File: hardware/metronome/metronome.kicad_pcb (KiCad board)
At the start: 2 copper layers, 59 x 34 mm, 57 parts, among them J1 USB_C_Receptacle_USB2.0, J2 Conn_01x03_Pin, J3 Conn_01x04_Pin, J4 AudioJack3_Ground, SW1 RotaryEncoder_Switch, SW2 SW_SPST, SW3 SW_SPST, SW4 SW_SPST, SW5 SW_SPST, U1 ATtiny412, U2 ME6209A40PG, U3 FM8002, Y1 10MHz

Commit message: Version 02
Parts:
- removed H1: MountingHole, MountingHole:MountingHole_2.2mm_M2
- added C13: 100uF, Capacitor_SMD:CP_Elec_6.3x5.4_Nichicon, F.Cu at (155.7, 67.0)
- added C14: 2.2uF, Capacitor_SMD:C_0805_2012Metric_Pad1.18x1.45mm_HandSolder, F.Cu at (136.7, 68.6)
- added C15: 0.1uF, Capacitor_SMD:C_0603_1608Metric_Pad1.08x0.95mm_HandSolder, F.Cu at (145.6, 61.7)
- added R30: 3k9, Resistor_SMD:R_0603_1608Metric_Pad0.98x0.95mm_HandSolder, F.Cu at (141.1, 63.5)
- added R31: 3k9, Resistor_SMD:R_0603_1608Metric_Pad0.98x0.95mm_HandSolder, F.Cu at (150.1, 70.6)
- added R32: 3k9, Resistor_SMD:R_0603_1608Metric_Pad0.98x0.95mm_HandSolder, F.Cu at (145.7, 70.6)
- C10: value 1.0uF -> 1uF
- C11: value 0.33uF -> 100uF; footprint Capacitor_SMD:C_0603_1608Metric_Pad1.08x0.95mm_HandSolder -> Capacitor_SMD:CP_Elec_6.3x5.4_Nichicon
- C12: value 1.0uF -> 2.2uF; footprint Capacitor_SMD:C_0603_1608Metric_Pad1.08x0.95mm_HandSolder -> Capacitor_SMD:C_0805_2012Metric_Pad1.18x1.45mm_HandSolder
- J2: value Conn_01x03_Pin -> Conn_01x04_Pin; footprint Connector_PinHeader_2.54mm:PinHeader_1x03_P2.54mm_Vertical -> ELonginus:1x4_2.54mm_pin_staggered
- J4: footprint ELonginus:Jack_3.5mm_PJ320E_Horizontal -> ELonginus:6.35mm headphone jack PJ-611A
- R26: value 10k -> 100k
- R27: value 20k -> 100k
- R28: value 20k -> 3k9
- SW2, SW3: footprint Button_Switch_THT:SW_PUSH_6mm_H4.3mm -> ELonginus:SW_PUSH_6mm
- SW4, SW5: footprint Button_Switch_THT:SW_PUSH-12mm -> ELonginus:SW_PUSH_12mm
- U3: value FM8002 -> LM4808; footprint Package_SO:SOP-8-1EP_4.57x4.57mm_P1.27mm_EP4.57x4.45mm_ThermalVias -> Package_SO:SOIC-8_3.9x4.9mm_P1.27mm
- moved C11 30.4 mm to (163.1, 67.0), turned to 90 degrees
- moved R21 19.1 mm to (150.0, 85.1), turned to 0 degrees
- moved C5 17.6 mm to (145.9, 85.1), turned to 180 degrees
- moved C12 15.3 mm to (136.7, 65.5), turned to 0 degrees
- moved R11 8.18 mm to (141.1, 70.6), turned to 0 degrees
- moved R28 6.70 mm to (145.7, 63.5), turned to 0 degrees
- moved R26 6.48 mm to (141.1, 67.1), turned to 0 degrees
- moved R27 6.40 mm to (141.1, 65.3), turned to 180 degrees
- moved C10 5.54 mm to (141.1, 68.8), turned to 180 degrees
- moved U3 4.05 mm to (147.8, 67.1)
- moved C4 3.74 mm to (136.8, 70.6)
- moved J4 1.46 mm to (164.7, 57.4)
- moved J2 1.40 mm to (150.2, 54.9)
- moved J1 0.65 mm to (112.9, 60.4)
- moved U1 0.38 mm to (140.1, 58.6)
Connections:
- C10 pad 1: Net-(U3-BYPASS) -> Net-(U3-INAP)
- C11 pad 1: AUDIO_OUT -> VOUT1
- C11 pad 2: Net-(C11-Pad2) -> BC1
- C12 pad 1: +3.3V -> AUDIO_OUT
- C12 pad 2: GND -> Net-(C12-Pad2)
- J4 pad R: VO1 -> BC1
- J4 pad T: VO2 -> BC2
- R26 pad 1: Net-(U3-SHTDN) -> +3.3V
- R26 pad 2: +3.3V -> Net-(U3-INAP)
- R27 pad 1: Net-(U3-IN-) -> Net-(U3-INAP)
- R27 pad 2: Net-(C11-Pad2) -> GND
- R28 pad 1: VO1 -> Net-(U3-INAN)
- R28 pad 2: Net-(U3-IN-) -> VOUT1
- U3 pad 1: Net-(U3-SHTDN) -> VOUT1
- U3 pad 2: Net-(U3-BYPASS) -> Net-(U3-INAN)
- U3 pad 3: Net-(U3-BYPASS) -> Net-(U3-INAP)
- U3 pad 4: Net-(U3-IN-) -> GND
- U3 pad 5: VO1 -> Net-(U3-INAP)
- U3 pad 6: +3.3V -> Net-(U3-INBN)
- U3 pad 7: GND -> VOUT2
- U3 pad 8: VO2 -> +3.3V
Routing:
- net GND: track 195.1 -> 116.9 mm, vias 5 -> 6
- net VO1: track 25.1 -> 0.00 mm, vias 1 -> 0
- net +3.3V: track 148.3 -> 172.6 mm
- net VOUT2: track 0.00 -> 22.5 mm, vias 0 -> 3
- net VOUT1: track 0.00 -> 21.3 mm, vias 0 -> 2
- net VO2: track 16.9 -> 0.00 mm
- net Net-(U3-INAP): track 0.00 -> 12.7 mm
- net AUDIO_OUT: track 13.9 -> 24.6 mm, vias 2 -> 3
- net Net-(U3-IN-): track 10.4 -> 0.00 mm
- net Net-(SW3-B): track 32.4 -> 23.5 mm
- net Net-(C14-Pad2): track 0.00 -> 8.95 mm, vias 0 -> 2
- net Net-(U3-INBN): track 0.00 -> 7.92 mm, vias 0 -> 2
- net Net-(U3-SHTDN): track 7.84 -> 0.00 mm
- net PA3: track 4.08 -> 11.5 mm
- net Net-(U3-INAN): track 0.00 -> 7.19 mm
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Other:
- board text added: "EZER LONGINUS MAR 2024"
- board text added: "METRONOME V0.2"
- board text removed: "EZER LONGINUS FEB 2024"
- board text removed: "METRONOME V0.1"

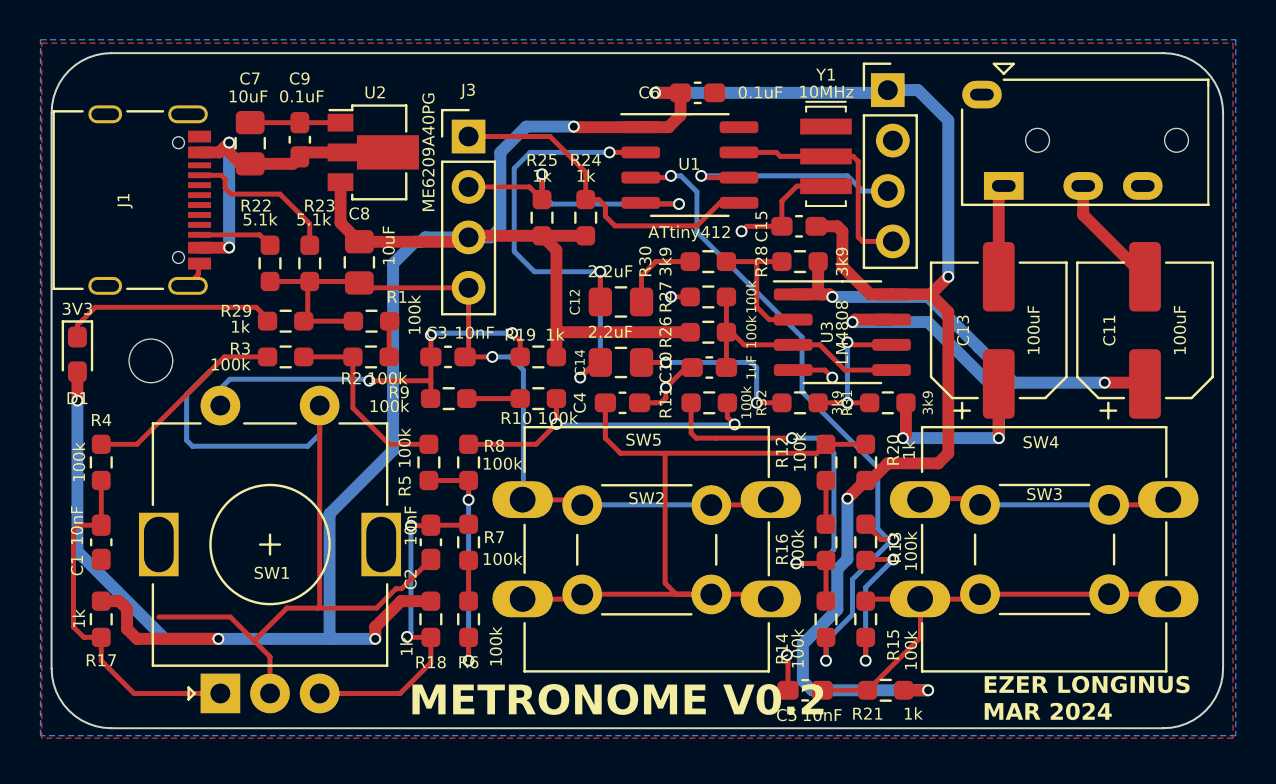
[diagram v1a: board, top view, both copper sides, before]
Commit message: pin swap
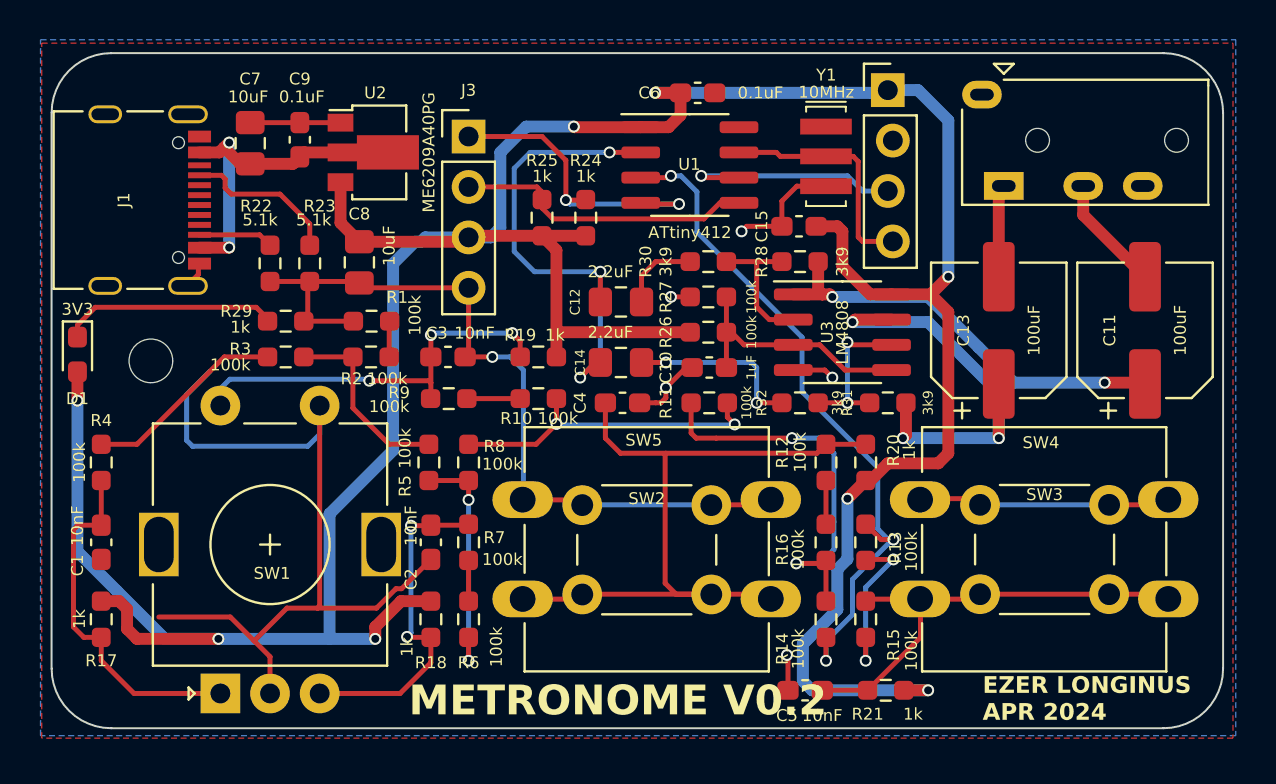
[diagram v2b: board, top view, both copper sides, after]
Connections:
- J3 pad 1: SCL -> SDA
- J3 pad 2: SDA -> SCL
- R24 pad 1: SCL -> SDA
- R25 pad 1: SDA -> SCL
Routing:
- net SCL: track 17.4 -> 15.5 mm
- net SDA: track 14.9 -> 15.8 mm
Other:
- board text added: "EZER LONGINUS APR 2024"
- board text removed: "EZER LONGINUS MAR 2024"
